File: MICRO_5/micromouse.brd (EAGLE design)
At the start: 100 x 80 mm, 34 parts

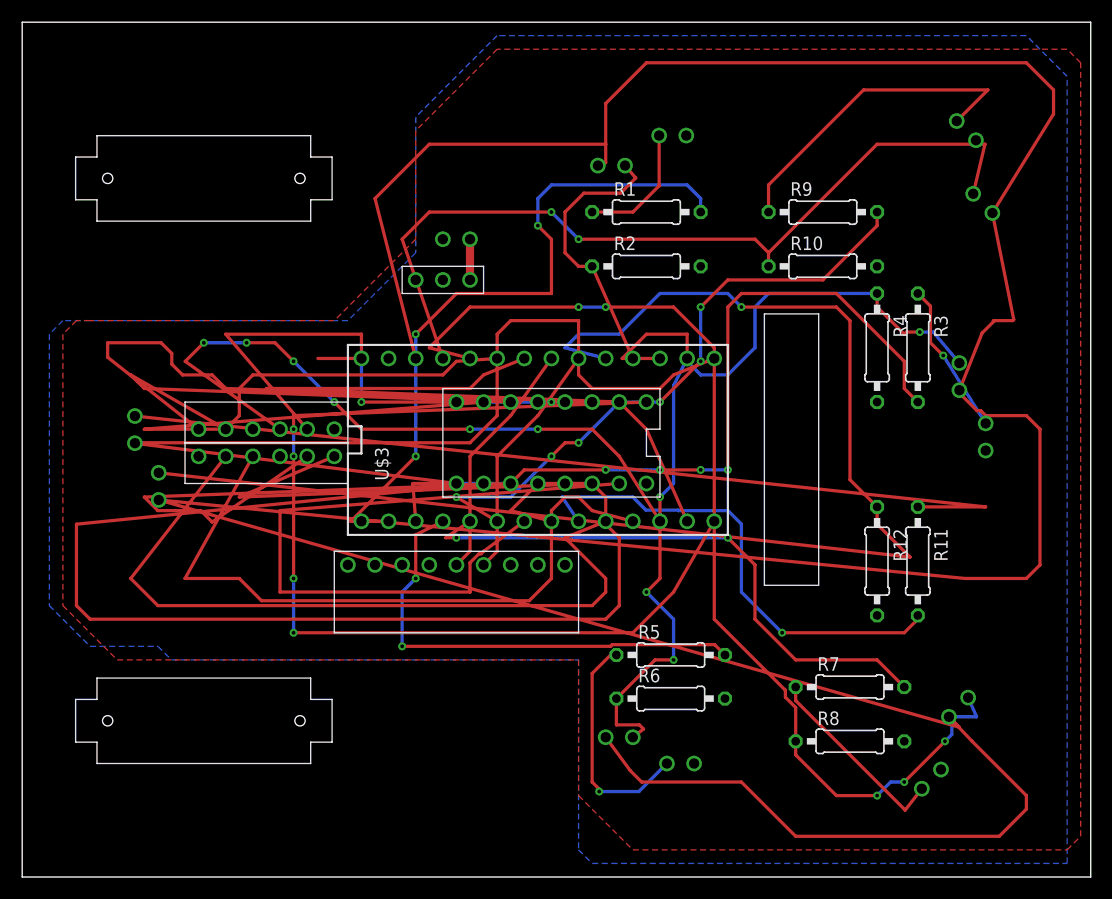
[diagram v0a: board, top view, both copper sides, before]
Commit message: made 45 degrees sensors into 20 degree sensors
so it stays in current cell for ir control. Put irs back so they fit on the board and won't stick out (need to double check). replaced middle resistors for more space. replaced motor brackets so they're as inward as possible but still able to fit onto the board with the new space available in the middle back
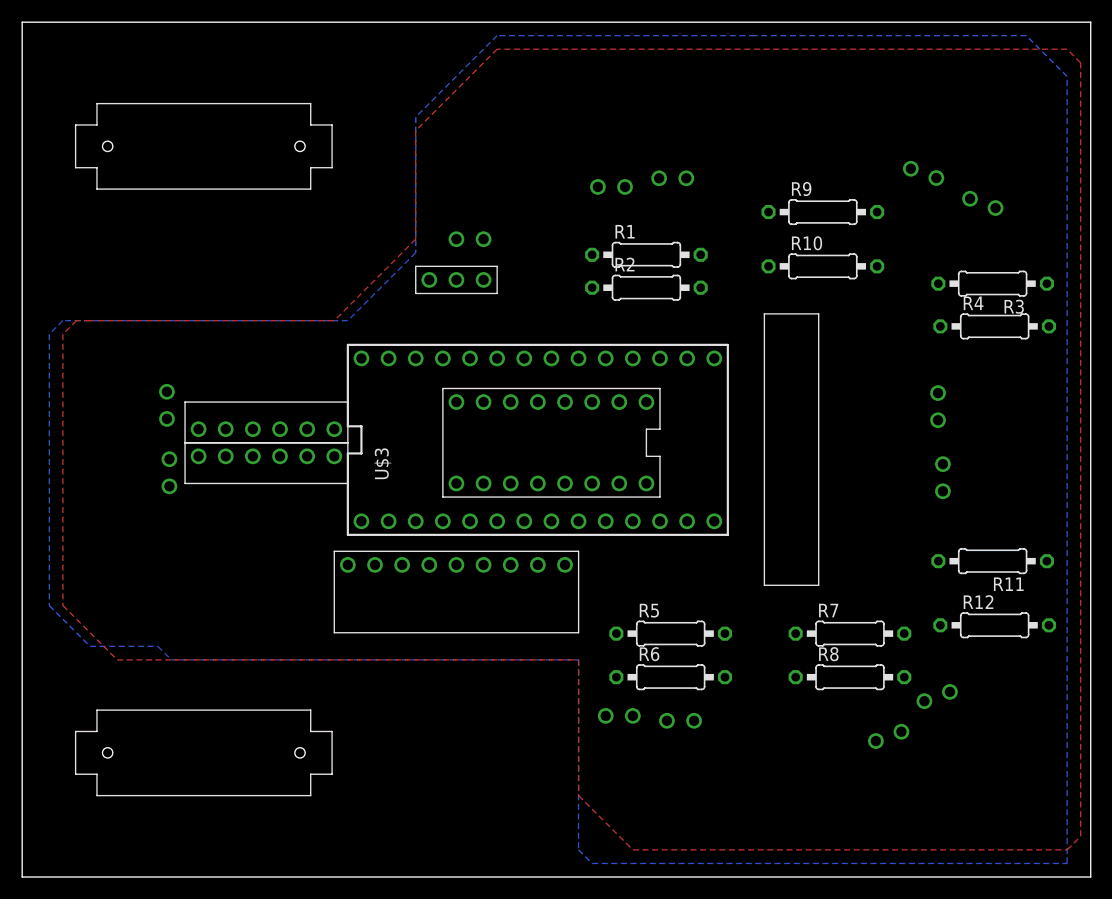
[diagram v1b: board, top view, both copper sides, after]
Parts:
- moved R12 12.5 mm to (91.0, 23.6), turned to 0 degrees
- moved R4 11.2 mm to (91.0, 51.5), turned to 0 degrees
- moved R3 9.22 mm to (90.8, 55.5), turned to 180 degrees
- moved R11 7.00 mm to (90.8, 29.6), turned to 180 degrees
- moved R8 6.00 mm to (77.5, 18.7)
- moved U$14 5.66 mm to (81.1, 13.2), turned to 20 degrees
- moved U$16 5.66 mm to (84.4, 65.8), turned to 340 degrees
- moved U$6 5.52 mm to (86.2, 37.4)
- moved R7 5.00 mm to (77.5, 22.8)
- moved R1 4.00 mm to (58.4, 58.2)
- moved U$7 4.00 mm to (61.6, 14.6)
- moved U$9 4.00 mm to (60.9, 65.4)
- moved U$22 3.76 mm to (13.6, 44.1)
- moved U$12 3.45 mm to (85.7, 44.0)
- moved U$18 3.00 mm to (17.0, 11.6)
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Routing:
- net 3.3V_VCC: track 363.4 -> 0.00 mm
- net N$14: track 129.0 -> 0.00 mm, vias 1 -> 0
- net M2_FWD_PWM: track 122.9 -> 0.00 mm
- net M2_ENABLE: track 101.0 -> 0.00 mm
- net N$8: track 99.5 -> 0.00 mm, vias 5 -> 0
- net N$4: track 98.1 -> 0.00 mm, vias 4 -> 0
- net N$13: track 86.4 -> 0.00 mm
- net N$12: track 79.2 -> 0.00 mm, vias 2 -> 0
- net N$22: track 72.8 -> 0.00 mm, vias 6 -> 0
- net OUTB_R: track 71.3 -> 0.00 mm
- net M1_REV_PWM: track 69.0 -> 0.00 mm
- net OUTB_L: track 67.9 -> 0.00 mm, vias 4 -> 0
- net N$5: track 66.4 -> 0.00 mm
- net N$19: track 64.8 -> 0.00 mm, vias 3 -> 0
- net OUTA_R: track 64.2 -> 0.00 mm
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
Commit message: cut out part near the motor so the motor can be closer in and be less likely to get stuck
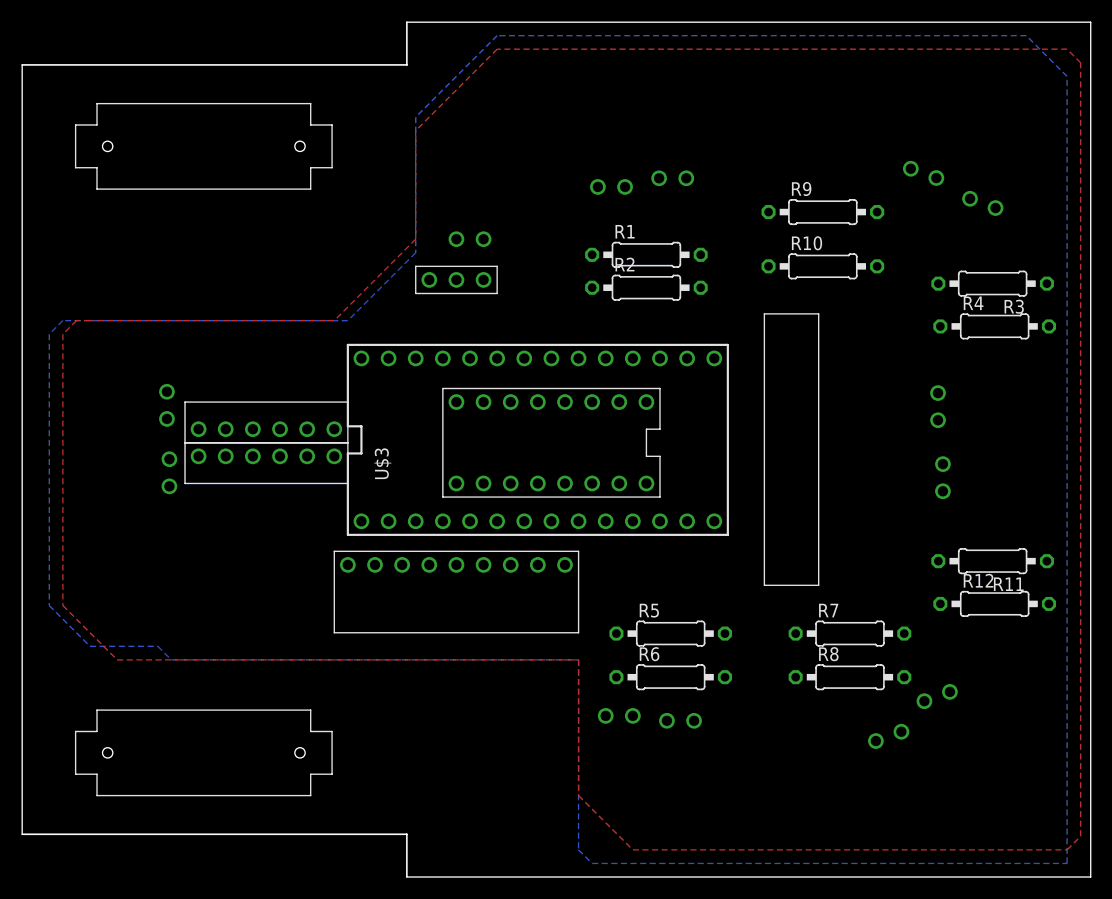
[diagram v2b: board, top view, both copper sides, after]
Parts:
- moved R12 2.00 mm to (91.0, 25.6)
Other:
- outline, holes or cut-outs redrawn
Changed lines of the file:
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@@
 <board>
 <plain>
-<wire x1="0" y1="0" x2="100" y2="0" width="0" layer="20"/>
+<wire x1="36" y1="0" x2="100" y2="0" width="0" layer="20"/>
 <wire x1="100" y1="0" x2="100" y2="80" width="0" layer="20"/>
-<wire x1="100" y1="80" x2="0" y2="80" width="0" layer="20"/>
-<wire x1="0" y1="80" x2="0" y2="0" width="0" layer="20"/>
+<wire x1="100" y1="80" x2="36" y2="80" width="0" layer="20"/>
+<wire x1="0" y1="76" x2="0" y2="4" width="0" layer="20"/>
+<wire x1="0" y1="76" x2="36" y2="76" width="0.1524" layer="20"/>
+<wire x1="36" y1="76" x2="36" y2="80" width="0.1524" layer="20"/>
+<wire x1="36" y1="0" x2="36" y2="4" width="0.1524" layer="20"/>
+<wire x1="36" y1="4" x2="0" y2="4" width="0.1524" layer="20"/>
 </plain>
 <attributes>
@@
 <attribute name="SPICEPREFIX" value="R" x="90.82" y="29.56" size="1.778" layer="27" rot="R180" display="off"/>
 </element>
-<element name="R12" library="rcl" library_urn="urn:adsk.eagle:library:334" package="0207/10" package3d_urn="urn:adsk.eagle:package:23491/1" value="10K" x="91.01" y="23.56">
-<attribute name="SPICEPREFIX" value="R" x="91.01" y="23.56" size="1.778" layer="27" display="off"/>
+<element name="R12" library="rcl" library_urn="urn:adsk.eagle:library:334" package="0207/10" package3d_urn="urn:adsk.eagle:package:23491/1" value="10K" x="91.01" y="25.56">
+<attribute name="SPICEPREFIX" value="R" x="91.01" y="25.56" size="1.778" layer="27" display="off"/>
 </element>
 <element name="R2" library="rcl" library_urn="urn:adsk.eagle:library:334" package="0207/10" package3d_urn="urn:adsk.eagle:package:23491/1" value="10K" x="58.42" y="55.15">
@@
 <contactref element="R12" pad="1"/>
 <contactref element="U$3" pad="17/A3"/>
-<wire x1="54.61" y1="48.53" x2="85.93" y2="23.56" width="0" layer="19" extent="1-1"/>
+<wire x1="54.61" y1="48.53" x2="85.93" y2="25.56" width="0" layer="19" extent="1-1"/>
 <wire x1="13.78" y1="39.1" x2="54.61" y2="48.53" width="0" layer="19" extent="1-1"/>
 </signal>

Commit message: cut out parts on all four sides of mouse so it can manuever better. Last thing is when led's come in is to double check measurements and correct them in pcb so they fit onto the board
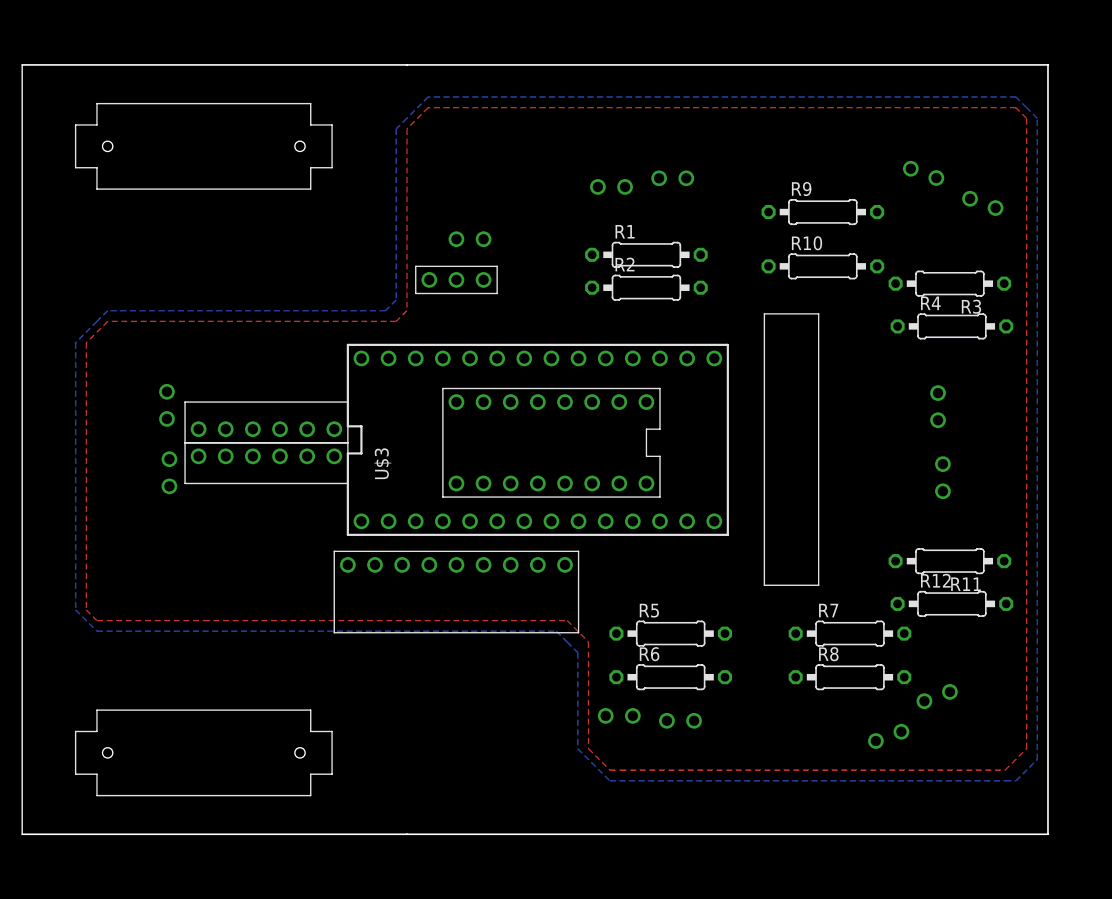
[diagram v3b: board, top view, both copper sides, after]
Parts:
- moved R11 4.00 mm to (86.8, 29.6)
- moved R12 4.00 mm to (87.0, 25.6)
- moved R3 4.00 mm to (86.8, 55.5)
- moved R4 4.00 mm to (87.0, 51.5)
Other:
- board size 100 x 80 mm -> 96 x 72 mm
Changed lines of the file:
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@@
 <board>
 <plain>
-<wire x1="36" y1="0" x2="100" y2="0" width="0" layer="20"/>
-<wire x1="100" y1="0" x2="100" y2="80" width="0" layer="20"/>
-<wire x1="100" y1="80" x2="36" y2="80" width="0" layer="20"/>
 <wire x1="0" y1="76" x2="0" y2="4" width="0" layer="20"/>
 <wire x1="0" y1="76" x2="36" y2="76" width="0.1524" layer="20"/>
-<wire x1="36" y1="76" x2="36" y2="80" width="0.1524" layer="20"/>
-<wire x1="36" y1="0" x2="36" y2="4" width="0.1524" layer="20"/>
 <wire x1="36" y1="4" x2="0" y2="4" width="0.1524" layer="20"/>
+<wire x1="36" y1="76" x2="96" y2="76" width="0.1524" layer="20"/>
+<wire x1="96" y1="76" x2="96" y2="4" width="0.1524" layer="20"/>
+<wire x1="96" y1="4" x2="36" y2="4" width="0.1524" layer="20"/>
 </plain>
 <attributes>
@@
 <attribute name="SPICEPREFIX" value="R" x="74.93" y="57.15" size="1.778" layer="27" display="off"/>
 </element>
-<element name="R11" library="rcl" library_urn="urn:adsk.eagle:library:334" package="0207/10" package3d_urn="urn:adsk.eagle:package:23491/1" value="330" x="90.82" y="29.56" rot="R180">
-<attribute name="SPICEPREFIX" value="R" x="90.82" y="29.56" size="1.778" layer="27" rot="R180" display="off"/>
-</element>
-<element name="R12" library="rcl" library_urn="urn:adsk.eagle:library:334" package="0207/10" package3d_urn="urn:adsk.eagle:package:23491/1" value="10K" x="91.01" y="25.56">
-<attribute name="SPICEPREFIX" value="R" x="91.01" y="25.56" size="1.778" layer="27" display="off"/>
+<element name="R11" library="rcl" library_urn="urn:adsk.eagle:library:334" package="0207/10" package3d_urn="urn:adsk.eagle:package:23491/1" value="330" x="86.82" y="29.56" rot="R180">
+<attribute name="SPICEPREFIX" value="R" x="86.82" y="29.56" size="1.778" layer="27" rot="R180" display="off"/>
+</element>
+<element name="R12" library="rcl" library_urn="urn:adsk.eagle:library:334" package="0207/10" package3d_urn="urn:adsk.eagle:package:23491/1" value="10K" x="87.01" y="25.56">
+<attribute name="SPICEPREFIX" value="R" x="87.01" y="25.56" size="1.778" layer="27" display="off"/>
 </element>
 <element name="R2" library="rcl" library_urn="urn:adsk.eagle:library:334" package="0207/10" package3d_urn="urn:adsk.eagle:package:23491/1" value="10K" x="58.42" y="55.15">
 <attribute name="SPICEPREFIX" value="R" x="58.42" y="55.15" size="1.778" layer="27" display="off"/>
 </element>
-<element name="R3" library="rcl" library_urn="urn:adsk.eagle:library:334" package="0207/10" package3d_urn="urn:adsk.eagle:package:23491/1" value="330" x="90.82" y="55.53" rot="R180">
-<attribute name="SPICEPREFIX" value="R" x="90.82" y="55.53" size="1.778" layer="27" rot="R180" display="off"/>
-</element>
-<element name="R4" library="rcl" library_urn="urn:adsk.eagle:library:334" package="0207/10" package3d_urn="urn:adsk.eagle:package:23491/1" value="10K" x="91.01" y="51.53">
-<attribute name="SPICEPREFIX" value="R" x="91.01" y="51.53" size="1.778" layer="27" display="off"/>
+<element name="R3" library="rcl" library_urn="urn:adsk.eagle:library:334" package="0207/10" package3d_urn="urn:adsk.eagle:package:23491/1" value="330" x="86.82" y="55.53" rot="R180">
+<attribute name="SPICEPREFIX" value="R" x="86.82" y="55.53" size="1.778" layer="27" rot="R180" display="off"/>
+</element>
+<element name="R4" library="rcl" library_urn="urn:adsk.eagle:library:334" package="0207/10" package3d_urn="urn:adsk.eagle:package:23491/1" value="10K" x="87.01" y="51.53">
+<attribute name="SPICEPREFIX" value="R" x="87.01" y="51.53" size="1.778" layer="27" display="off"/>
 </element>
 <element name="R5" library="rcl" library_urn="urn:adsk.eagle:library:334" package="0207/10" package3d_urn="urn:adsk.eagle:package:23491/1" value="330" x="60.69" y="22.78">
@@
 <contactref element="U$13" pad="VIN"/>
 <polygon width="0.1524" layer="1">
-<vertex x="3.81" y="50.8"/>
-<vertex x="3.81" y="25.4"/>
-<vertex x="7.62" y="21.59"/>
-<vertex x="8.89" y="20.32"/>
-<vertex x="52.07" y="20.32"/>
-<vertex x="52.07" y="7.62"/>
-<vertex x="57.15" y="2.54"/>
-<vertex x="97.79" y="2.54"/>
-<vertex x="99.06" y="3.81"/>
-<vertex x="99.06" y="76.2"/>
-<vertex x="97.79" y="77.47"/>
-<vertex x="44.45" y="77.47"/>
-<vertex x="36.83" y="69.85"/>
-<vertex x="36.83" y="59.69"/>
-<vertex x="33.02" y="55.88"/>
-<vertex x="29.21" y="52.07"/>
-<vertex x="6.35" y="52.07"/>
-<vertex x="5.08" y="52.07"/>
+<vertex x="6" y="50"/>
+<vertex x="6" y="25"/>
+<vertex x="7" y="24"/>
+<vertex x="17" y="24"/>
+<vertex x="51" y="24"/>
+<vertex x="53" y="22"/>
+<vertex x="53" y="12"/>
+<vertex x="55" y="10"/>
+<vertex x="56" y="10"/>
+<vertex x="92" y="10"/>
+<vertex x="94" y="12"/>
+<vertex x="94" y="71"/>
+<vertex x="93" y="72"/>
+<vertex x="38" y="72"/>
+<vertex x="36" y="70"/>
+<vertex x="36" y="53"/>
+<vertex x="35" y="52"/>
+<vertex x="8" y="52"/>
 </polygon>
 </signal>
@@
 <contactref element="U$3" pad="1"/>
 <contactref element="R3" pad="2"/>
-<wire x1="36.83" y1="33.29" x2="85.74" y2="55.53" width="0" layer="19" extent="1-1"/>
+<wire x1="36.83" y1="33.29" x2="81.74" y2="55.53" width="0" layer="19" extent="1-1"/>
 </signal>
 <signal name="N$23">
 <contactref element="R3" pad="1"/>
 <contactref element="U$6" pad="EMI_ANO"/>
-<wire x1="86.17" y1="38.64" x2="95.9" y2="55.53" width="0" layer="19" extent="1-1"/>
+<wire x1="86.17" y1="38.64" x2="91.9" y2="55.53" width="0" layer="19" extent="1-1"/>
 </signal>
 <signal name="N$25">
@@
 <contactref element="R4" pad="1"/>
 <contactref element="U$3" pad="15/A1"/>
-<wire x1="85.93" y1="51.53" x2="85.71" y2="45.29" width="0" layer="19" extent="1-1"/>
-<wire x1="59.69" y1="48.53" x2="85.93" y2="51.53" width="0" layer="19" extent="1-1"/>
+<wire x1="85.71" y1="45.29" x2="81.93" y2="51.53" width="0" layer="19" extent="1-1"/>
+<wire x1="59.69" y1="48.53" x2="81.93" y2="51.53" width="0" layer="19" extent="1-1"/>
 </signal>
 <signal name="N$28">
@@
 <contactref element="R7" pad="1"/>
 <contactref element="U$14" pad="EMI_ANO"/>
-<wire x1="72.39" y1="22.78" x2="79.8965875" y2="12.725634375" width="0" layer="19" extent="1-1"/>
+<wire x1="79.8965875" y1="12.725634375" x2="72.39" y2="22.78" width="0" layer="19" extent="1-1"/>
 </signal>
 <signal name="N$9">
@@
 <contactref element="R11" pad="2"/>
 <contactref element="U$3" pad="7"/>
-<wire x1="52.07" y1="33.29" x2="85.74" y2="29.56" width="0" layer="19" extent="1-1"/>
+<wire x1="52.07" y1="33.29" x2="81.74" y2="29.56" width="0" layer="19" extent="1-1"/>
 </signal>
 <signal name="N$13">
 <contactref element="R11" pad="1"/>
 <contactref element="U$22" pad="EMI_ANO"/>
-<wire x1="13.55" y1="45.41" x2="95.9" y2="29.56" width="0" layer="19" extent="1-1"/>
+<wire x1="13.55" y1="45.41" x2="91.9" y2="29.56" width="0" layer="19" extent="1-1"/>
 </signal>
 <signal name="N$14">
@@
 <contactref element="R12" pad="1"/>
 <contactref element="U$3" pad="17/A3"/>
-<wire x1="54.61" y1="48.53" x2="85.93" y2="25.56" width="0" layer="19" extent="1-1"/>
+<wire x1="54.61" y1="48.53" x2="81.93" y2="25.56" width="0" layer="19" extent="1-1"/>
 <wire x1="13.78" y1="39.1" x2="54.61" y2="48.53" width="0" layer="19" extent="1-1"/>
 </signal>
@@
 <contactref element="R10" pad="2"/>
 <polygon width="0.1524" layer="16">
-<vertex x="3.81" y="52.07"/>
-<vertex x="2.54" y="50.8"/>
-<vertex x="2.54" y="25.4"/>
-<vertex x="5.08" y="22.86"/>
-<vertex x="6.35" y="21.59"/>
-<vertex x="12.7" y="21.59"/>
-<vertex x="13.97" y="20.32"/>
-<vertex x="52.07" y="20.32"/>
-<vertex x="52.07" y="2.54"/>
-<vertex x="53.34" y="1.27"/>
-<vertex x="97.79" y="1.27"/>
-<vertex x="97.79" y="74.93"/>
-<vertex x="93.98" y="78.74"/>
-<vertex x="68.58" y="78.74"/>
-<vertex x="44.45" y="78.74"/>
-<vertex x="43.18" y="77.47"/>
-<vertex x="36.83" y="71.12"/>
-<vertex x="36.83" y="68.58"/>
-<vertex x="36.83" y="58.42"/>
-<vertex x="30.48" y="52.07"/>
-<vertex x="27.94" y="52.07"/>
+<vertex x="7" y="52"/>
+<vertex x="5" y="50"/>
+<vertex x="5" y="25"/>
+<vertex x="7" y="23"/>
+<vertex x="50" y="23"/>
+<vertex x="51" y="22"/>
+<vertex x="52" y="21"/>
+<vertex x="52" y="12"/>
+<vertex x="55" y="9"/>
+<vertex x="92" y="9"/>
+<vertex x="93" y="9"/>
+<vertex x="95" y="11"/>
+<vertex x="95" y="71"/>
+<vertex x="94" y="72"/>
+<vertex x="93" y="73"/>
+<vertex x="38" y="73"/>
+<vertex x="36" y="71"/>
+<vertex x="35" y="70"/>
+<vertex x="35" y="54"/>
+<vertex x="34" y="53"/>
+<vertex x="8" y="53"/>
 </polygon>
 </signal>
